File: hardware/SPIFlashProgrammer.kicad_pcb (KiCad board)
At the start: 4 copper layers, 54.3 x 24 mm, 64 parts, among them J1 Conn_02x04_Counter_Clockwise, J2 Conn_02x05_Odd_Even, Q1 DMN65D8L-7, Q2 DMN65D8L-7, Q3 2N7002DW, Q4 DMN65D8L-7, SW1 B3U-1000P-B, SW2 B3U-1000P-B, U1 TM4C123GH6PM, U2 FXL4TD245BQX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

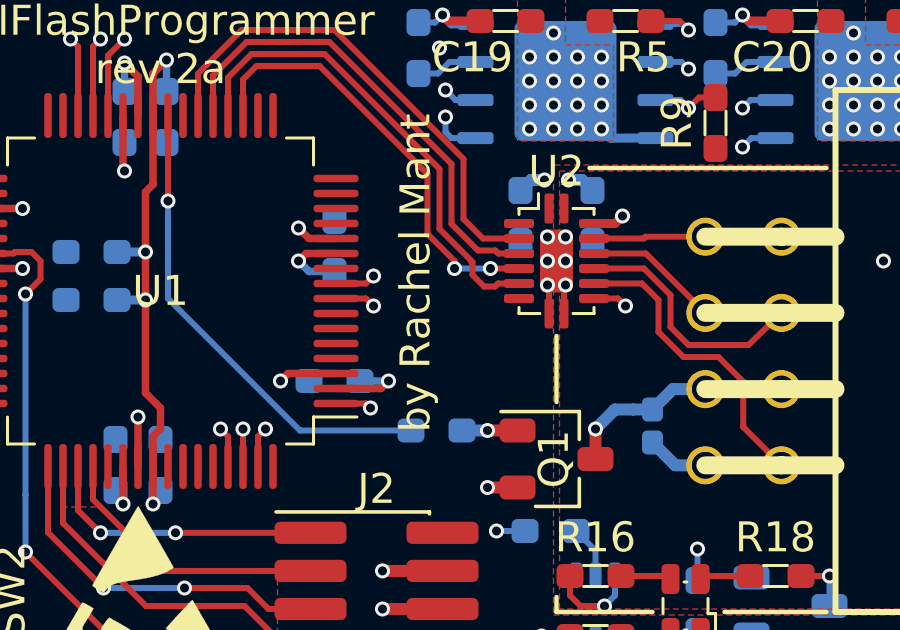
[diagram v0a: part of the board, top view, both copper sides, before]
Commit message: Added control for the level shifter output enable to the CPU to fix problems caused by us accidentally still driving the external bus after reset is released
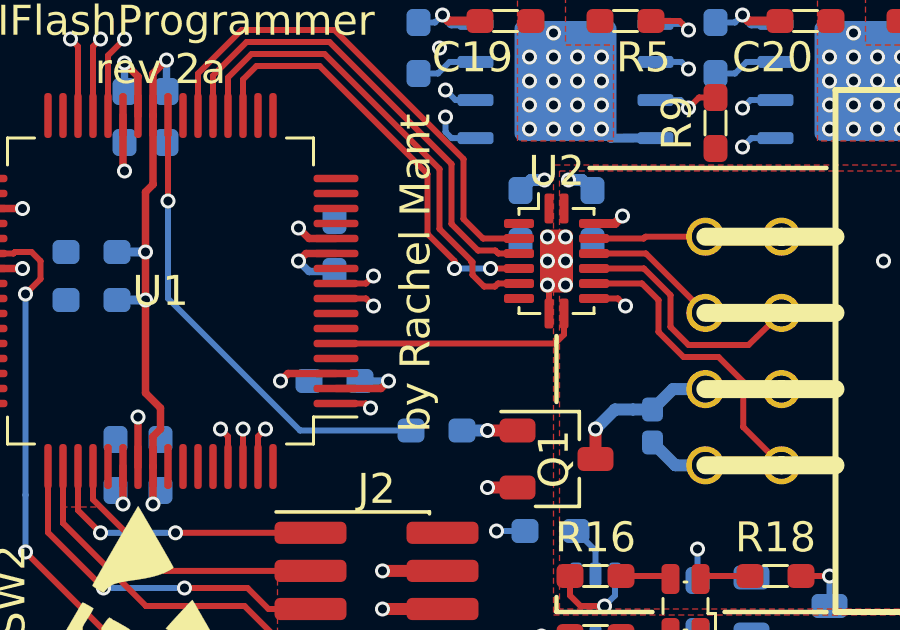
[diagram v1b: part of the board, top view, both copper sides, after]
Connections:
- net /Processor/FLASH_CLK renamed /Onboard Flash/SCK
- J1 pad 5: Net-(J1-Pad5) -> unconnected-(J1-Pad5)
- J2 pad 7: Net-(J2-Pad7) -> unconnected-(J2-Pad7)
- U1 pad 10: Net-(U1-Pad10) -> unconnected-(U1-Pad10)
- U1 pad 13: Net-(U1-Pad13) -> unconnected-(U1-Pad13)
- U1 pad 14: Net-(U1-Pad14) -> unconnected-(U1-Pad14)
- U1 pad 15: Net-(U1-Pad15) -> unconnected-(U1-Pad15)
- U1 pad 16: Net-(U1-Pad16) -> unconnected-(U1-Pad16)
- U1 pad 17: Net-(U1-Pad17) -> unconnected-(U1-Pad17)
- U1 pad 18: Net-(U1-Pad18) -> unconnected-(U1-Pad18)
- U1 pad 23: Net-(U1-Pad23) -> unconnected-(U1-Pad23)
- U1 pad 31: Net-(U1-Pad31) -> unconnected-(U1-Pad31)
- U1 pad 32: Net-(U1-Pad32) -> unconnected-(U1-Pad32)
- U1 pad 33: Net-(U1-Pad33) -> unconnected-(U1-Pad33)
- U1 pad 34: Net-(U1-Pad34) -> unconnected-(U1-Pad34)
- U1 pad 36: Net-(U1-Pad36) -> unconnected-(U1-Pad36)
- U1 pad 4: Net-(U1-Pad4) -> unconnected-(U1-Pad4)
- U1 pad 41: Net-(U1-Pad41) -> unconnected-(U1-Pad41)
- U1 pad 5: Net-(U1-Pad5) -> /Connectors/~{SPI_OE}
- U1 pad 53: Net-(U1-Pad53) -> unconnected-(U1-Pad53)
- U1 pad 57: Net-(U1-Pad57) -> unconnected-(U1-Pad57)
- U1 pad 58: Net-(U1-Pad58) -> unconnected-(U1-Pad58)
- U1 pad 59: Net-(U1-Pad59) -> unconnected-(U1-Pad59)
- U1 pad 6: Net-(U1-Pad6) -> unconnected-(U1-Pad6)
- U1 pad 60: Net-(U1-Pad60) -> unconnected-(U1-Pad60)
- U1 pad 64: Net-(U1-Pad64) -> unconnected-(U1-Pad64)
- U1 pad 7: Net-(U1-Pad7) -> unconnected-(U1-Pad7)
- U2 pad 9: GND -> /Connectors/~{SPI_OE}
- X1 pad 1: Net-(X1-Pad1) -> unconnected-(X1-Pad1)
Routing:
- net /Connectors/~{SPI_OE}: track 0.00 -> 8.42 mm
- net GND: track 29.4 -> 28.5 mm
